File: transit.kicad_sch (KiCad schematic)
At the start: 70 parts, among them J1 USB_C_Receptacle_USB2.0_16P, J2 Conn_01x03, SW1 RESET, SW2 BOOT, U1 ESP32-C3-MINI-1, U2 SPX3819M5-L-3-3, U3 USBLC6-2SC6, U4 SN74LVC8T245PWR, U5 TPU3013S5, U6 BH1603FVC-TR

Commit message: PCBA prototype order
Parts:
- C11: renamed from C8; footprint EasyEDA:C0805 -> EasyEDA:C0603; LCSC Part C95841 -> C15849
- C12: renamed from C9; footprint EasyEDA:C0805 -> EasyEDA:C0603; LCSC Part C95841 -> C15849
- C15: renamed from C12; footprint EasyEDA:C0805 -> EasyEDA:C0603; LCSC Part C95841 -> C15849
- C8: renamed from C13; footprint EasyEDA:C0805 -> EasyEDA:C0603; LCSC Part C95841 -> C15849
- SW1: value RESET -> SW_SPST; Function (none) -> RESET
- SW2: value BOOT -> SW_SPST; Function (none) -> BOOT
- renumbered C7 to C10, C10 to C13, C11 to C14, C15 to C6, C14 to C7, C6 to C9
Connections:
- net USBCC1: now also J1.A5 (CC1), R4.1
- net USBCC2: now also J1.B5 (CC2), R3.1
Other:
- moved on the sheet: C1, C2, C6, C7, R1, R2, TP3, U1

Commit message: Rev B component layout
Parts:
- removed C12, C15: 1u, EasyEDA:C0603, symbol EasyEDA:CL21B106KOQNNNE
- removed C13: 100n, EasyEDA:C0603, symbol EasyEDA:CL10B104KB8NNNC
- removed H8: ~, MountingHole:MountingHole_3.2mm_M3_DIN965_Pad, symbol Mechanical:MountingHole_Pad
- removed R18, R19, R22: 100K, EasyEDA:R0603, symbol EasyEDA:0603WAF1002T5E
- removed R2: 10K, EasyEDA:R0603, symbol EasyEDA:0603WAF1002T5E
- removed R20, R21: 100R, EasyEDA:R0603, symbol EasyEDA:0603WAF1002T5E
- removed TP10: Rail-E-MCU, TestPoint:TestPoint_Keystone_5005-5009_Compact, symbol Connector:TestPoint
- removed TP6: LVL-Shifter-EN, TestPoint:TestPoint_Keystone_5005-5009_Compact, symbol Connector:TestPoint
- removed TP7: Ferries-S-MCU, TestPoint:TestPoint_Keystone_5005-5009_Compact, symbol Connector:TestPoint
- removed TP8: Ferries-N-MCU, TestPoint:TestPoint_Keystone_5005-5009_Compact, symbol Connector:TestPoint
- removed TP9: Rail-W-MCU, TestPoint:TestPoint_Keystone_5005-5009_Compact, symbol Connector:TestPoint
- removed U4: SN74LVC8T245PWR, EasyEDA:TSSOP-24_L7.8-W4.4-P0.65-LS6.4-BL, symbol EasyEDA:SN74LVC8T245PWR
- added C13, C16: 1u, EasyEDA:C0603, symbol EasyEDA:CL21B106KOQNNNE
- added C15: 100n, EasyEDA:C0603, symbol EasyEDA:CL10B104KB8NNNC
- added C3: 47u, EasyEDA:C0805, symbol EasyEDA:CL21A476MQYNNNE
- added D2, D3, D4: SS34, EasyEDA:D_SMA, symbol EasyEDA:SS34_C8678
- added J2: USB_C_Receptacle_USB2.0_16P, Connector_USB:USB_C_Receptacle_GCT_USB4105-xx-A_16P_TopMnt_Horizontal, symbol Connector:USB_C_Receptacle_USB2.0_16P
- added LED3: BLUE, EasyEDA:LED0805-R-RD, symbol Device:LED_Small
- added R18: 2K2, EasyEDA:R0603, symbol Device:R
- added SW3: SW_SPST, EasyEDA:KEY-SMD_L6.2-W3.6-LS8.0_K2-1107ST-A4SW-06, symbol Switch:SW_SPST
- added U7: SN74LVC2T45DCUR, EasyEDA:VSSOP-8_2.3x2mm_P0.5mm, symbol EasyEDA:SN74LVC2T45DCUR
- C11: renamed from C10; value 47u -> 22u; footprint EasyEDA:C1206 -> EasyEDA:C0805; LCSC Part C96123 -> C45783
- H1, H2, H3, H4, H5, H6, H7: value ~ -> (none)
- R13, R14: value 10K -> 100R; LCSC Part C25804 -> C22775
- R15: value 100R -> 5K1; LCSC Part C22775 -> C23186
- R16: value 100K -> 5K1; LCSC Part C25803 -> C23186
- R17: value 100R -> 10K; LCSC Part C22775 -> C25804
- U2: value SPX3819M5-L-3-3 -> TLV75733PDYDR; footprint EasyEDA:SOT-23-5_L3.0-W1.6-P0.95-LS2.8-BR -> EasyEDA:Texas_DYD0005A_SOT-23-5-EP; symbol Regulator_Linear:SPX3819M5-L-3-3 -> EasyEDA:TLV75733PDYDR; LCSC Part C20617301 -> C22399950
- renumbered C2 to C1, C9 to C10, C11 to C12, C1 to C2, C3 to C4, C4 to C5, C5 to C6, C6 to C7, C7 to C8, C8 to C9, J2 to J3, R11 to R10, R12 to R11, R23 to R12, R3 to R2, R4 to R3, R5 to R4, R6 to R5, R7 to R6, R8 to R7, R9 to R8, R10 to R9
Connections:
- net Ferries_N_Bus is gone; now on net GND: R15.2
- net Rail_E_MCU is gone; now on net WiFi_LED: U1.13 (GPIO1/ADC1_CH1/XTAL_32K_N)
- net Rail_W_MCU is gone; now on net Bright_CTL: U1.16 (GPIO10)
- net +3V3: now also C14.2, R17.1, C13.1, C3.1, U7.1 (VCCA), U7.5 (DIR); no longer R13.1, R14.1
- net +VLED: now also C15.2, C16.1, U7.8 (VCCB); no longer C14.2
- net ESP32_BOOT: no longer R13.2
- net Ferries S: now also R13.2; no longer R17.1
- net GND: now also C13.2, C15.1, C16.2, C3.2, J2.A1 (GND), J2.A12 (GND), J2.B1 (GND), J2.B12 (GND), J2.S1 (SHIELD), LED3.1 (K), SW3.2 (B), U7.4 (GND)
- net Rail W: now also R14.2
- net WiFi_LED: no longer U1.12 (GPIO0/ADC1_CH0/XTAL_32K_P)
- net at J1.A4 (VBUS), J1.A9 (VBUS), J1.B4 (VBUS)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: now also D2.2 (A); no longer D1.2, F1.1, U3.5 (VBUS)
- net Ferries N renamed USB_PWR_CC1
- net USB_PWR_CC1: now also J2.A5 (CC1); no longer R15.1
- net Ferries_N_MCU renamed Ferries_MCU
- net Ferries_MCU: now also U7.2 (A1)
- net Ferries_S_Bus renamed Bright_CTL
- net Bright_CTL: now also SW3.1 (A)
- net Ferries_S_MCU renamed Rail_MCU
- net Rail_MCU: now also U7.3 (A2)
- net LVL_Shifter_EN_Active_Low: no longer names the net of U1.21 (GPIO7)
- net LVL_Shifter_EN_Active_Low: no longer R14.2
- new net: D3.2 (A), D4.2 (A), J2.A4 (VBUS), J2.A9 (VBUS), J2.B4 (VBUS), J2.B9 (VBUS)
- new net: LED3.2 (A), R18.1
- new net Data_LED: R18.2, U1.12 (GPIO0/ADC1_CH0/XTAL_32K_P)
- new net Ferries_LED: R13.1, U7.7 (B1)
- new net Rail_LED: R14.1, U7.6 (B2)
- new net USB_PWR_CC2: J2.B5 (CC2), R15.1
- new net VBUS_RAW: D1.2, D2.1 (K), D3.1 (K), D4.1 (K), F1.1, U3.5 (VBUS)
- no-connect marks 6 -> 14
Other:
- removed sheet Ferries N
- removed sheet Ferries S
- removed sheet Rail E
- removed sheet Rail W
- added sheet Ferries (ferries.kicad_sch)
- added sheet Rail (rail.kicad_sch)
- note added: "Brightness Button"
- note added: "DIR=1 A data to B Bus"
- note added: "Data LED"
- note added: "USB-C Connector (Power + Data)"
- note added: "USB-C Connector (Power only)"
- note removed: "A data to B Bus OE=0, DIR=1"
- note removed: "To ensure the high- impedance state during power up or power down, OE should be tied to VCC through a pullup resistor"
- note removed: "USB-C Connector"
- company: Charles Street Labs -> Salt River Labs
- moved on the sheet: D1, F1, H1, H2, H3, H4, H5, H6, J1, J3, LED2, R12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

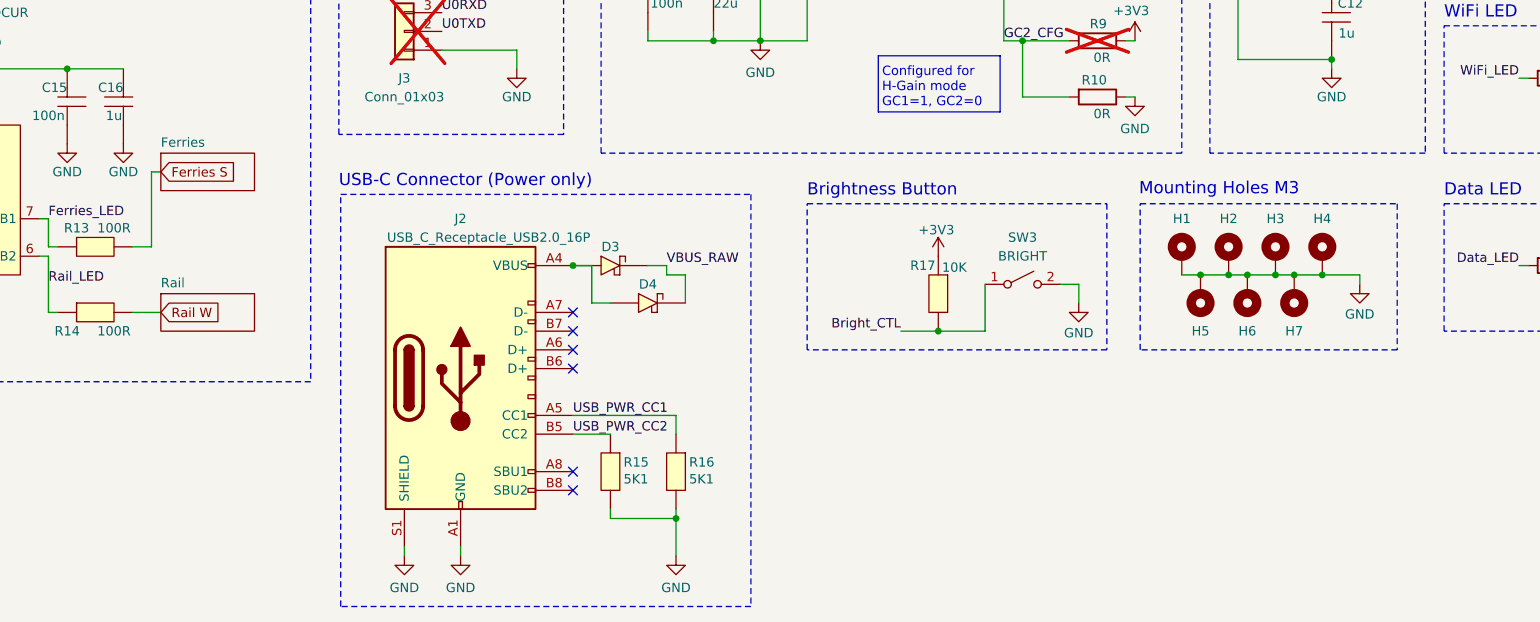
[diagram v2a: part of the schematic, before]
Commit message: Add basemap, rerouting checkpoint
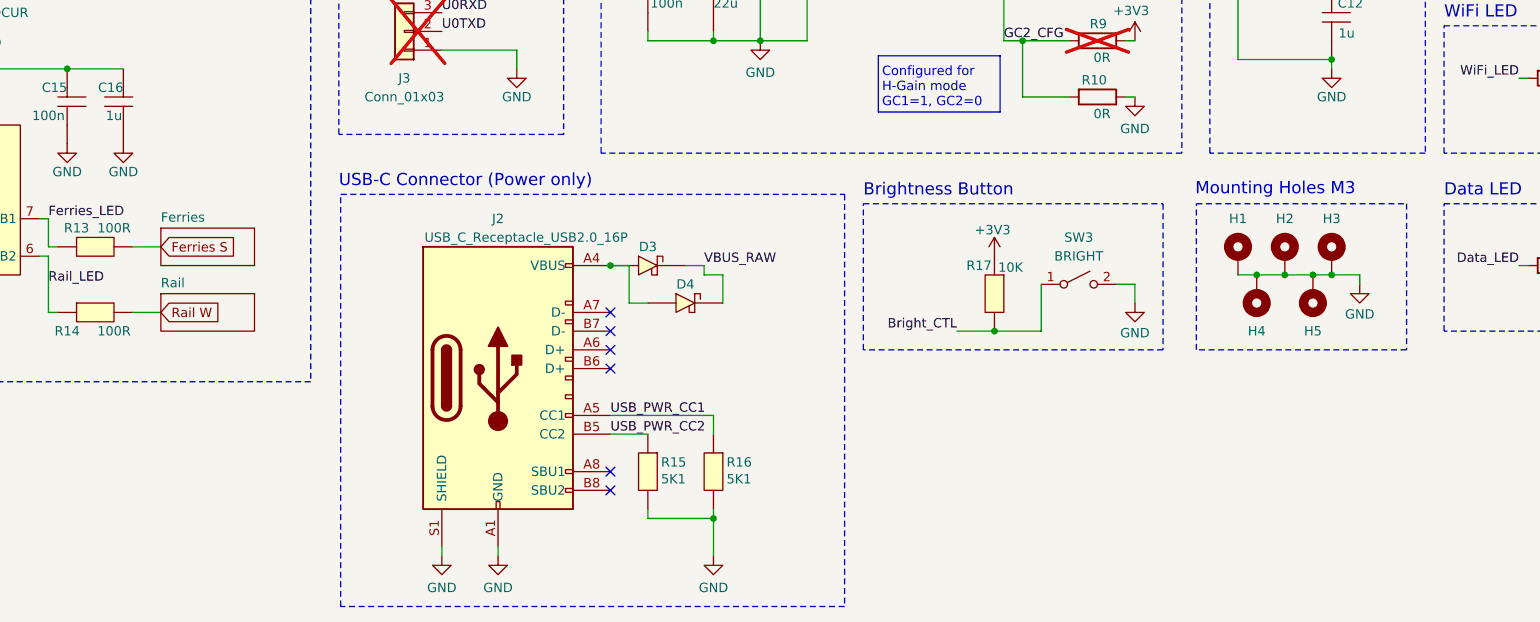
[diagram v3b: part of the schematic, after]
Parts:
- removed H6, H7: (no value), MountingHole:MountingHole_3.2mm_M3_DIN965_Pad, symbol Mechanical:MountingHole_Pad
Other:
- moved on the sheet: D3, D4, H1, H2, H3, J2, R15, R16, R17, SW3

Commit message: checkpoint before label plugin
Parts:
- SW2: Function BOOT -> MODE
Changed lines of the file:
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@@
 			)
 		)
-		(property "Function" "BOOT"
+		(property "Function" "MODE"
 			(at 257.81 97.79 0)
 			(show_name no)

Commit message: Route main circuit
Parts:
- J1, J2: footprint Connector_USB:USB_C_Receptacle_GCT_USB4105-xx-A_16P_TopMnt_Horizontal -> Transit:USB_C_Receptacle_GCT_USB4105-xx-A_16P_TopMnt_Horizontal
- TP1, TP2, TP3, TP4, TP5: footprint TestPoint:TestPoint_Keystone_5005-5009_Compact -> TestPoint:TestPoint_Keystone_5000-5004_Miniature
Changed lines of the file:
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@@
 			)
 		)
-		(property "Footprint" "Connector_USB:USB_C_Receptacle_GCT_USB4105-xx-A_16P_TopMnt_Horizontal"
+		(property "Footprint" "Transit:USB_C_Receptacle_GCT_USB4105-xx-A_16P_TopMnt_Horizontal"
 			(at 123.19 163.83 0)
 			(hide yes)
@@
 			)
 		)
-		(property "Footprint" "TestPoint:TestPoint_Keystone_5005-5009_Compact"
+		(property "Footprint" "TestPoint:TestPoint_Keystone_5000-5004_Miniature"
 			(at 264.16 26.67 0)
 			(hide yes)
@@
 			)
 		)
-		(property "Footprint" "TestPoint:TestPoint_Keystone_5005-5009_Compact"
+		(property "Footprint" "TestPoint:TestPoint_Keystone_5000-5004_Miniature"
 			(at 234.95 64.77 0)
 			(hide yes)
@@
 			)
 		)
-		(property "Footprint" "TestPoint:TestPoint_Keystone_5005-5009_Compact"
+		(property "Footprint" "TestPoint:TestPoint_Keystone_5000-5004_Miniature"
 			(at 147.32 99.06 0)
 			(hide yes)
@@
 			)
 		)
-		(property "Footprint" "TestPoint:TestPoint_Keystone_5005-5009_Compact"
+		(property "Footprint" "TestPoint:TestPoint_Keystone_5000-5004_Miniature"
 			(at 193.04 29.21 0)
 			(hide yes)
@@
 			)
 		)
-		(property "Footprint" "TestPoint:TestPoint_Keystone_5005-5009_Compact"
+		(property "Footprint" "TestPoint:TestPoint_Keystone_5000-5004_Miniature"
 			(at 273.05 68.58 0)
 			(hide yes)
@@
 			)
 		)
-		(property "Footprint" "Connector_USB:USB_C_Receptacle_GCT_USB4105-xx-A_16P_TopMnt_Horizontal"
+		(property "Footprint" "Transit:USB_C_Receptacle_GCT_USB4105-xx-A_16P_TopMnt_Horizontal"
 			(at 160.02 52.07 0)
 			(hide yes)

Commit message: route link 1
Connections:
- net Rail W renamed RAIL
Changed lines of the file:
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@@
 		)
 	)
-	(global_label "Rail W"
+	(global_label "RAIL"
 		(shape input)
 		(at 73.66 154.94 0)
@@
 		)
 		(property "Intersheetrefs" "${INTERSHEET_REFS}"
-			(at 82.7532 154.94 0)
+			(at 80.6367 154.94 0)
 			(hide yes)
 			(show_name no)

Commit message: Route point defiance tahlequah
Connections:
- net Ferries S renamed FERRY
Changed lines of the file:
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@@
 		)
 	)
-	(global_label "Ferries S"
+	(global_label "FERRY"
 		(shape input)
 		(at 73.66 146.05 0)
@@
 		)
 		(property "Intersheetrefs" "${INTERSHEET_REFS}"
-			(at 85.2934 146.05 0)
+			(at 82.5114 146.05 0)
 			(hide yes)
 			(show_name no)

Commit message: rev-b validation run
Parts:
- removed D4: SS34, EasyEDA:D_SMA, symbol EasyEDA:SS34_C8678
- added TP10, TP12, TP6, TP7, TP8, TP9: Ambient-Light-SNS, TestPoint:TestPoint_Keystone_5000-5004_Miniature, symbol Connector:TestPoint
- added TP11: +VBUS, TestPoint:TestPoint_Keystone_5000-5004_Miniature, symbol Connector:TestPoint
- renumbered U5 to U4, U6 to U5, U7 to U6
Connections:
- net ESP32_BOOT: now also TP8.1
- net ESP32_EN: now also TP7.1
- net FERRY: now also TP9.1
- net GND: now also TP11.1, TP12.1
- net RAIL: now also TP10.1
- net VBUS_RAW: now also TP6.1
- no-connect marks 14 -> 13
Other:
- moved on the sheet: F1, R11
